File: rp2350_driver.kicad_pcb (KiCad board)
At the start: 6 copper layers, 76 x 44.4 mm, 194 parts, among them J19 Conn_01x03, J201 Estop Conn, J202 USB_C_Receptacle_USB2.0, J203 Conn_01x06, J204 SM03B-SRSS-TB, J206 SM03B-SRSS-TB, J21 Power Input, Q1 Q_PNP_BEC, Q2 Q_PNP_BEC, Q3 Q_PNP_BEC, SW201 Boot, SW202 Reset, U1 INA240A1D, U2 EG3113, U202 SPX3819M5-L-3-3, U203 RP2350_80QFN, U204 W25Q16JV, U205 USBLC6-4SC6, U21 INA240A1D, U44 INA240A1D, U5 EG3113, U8 EG3113, Y201 ABM8-272-T3

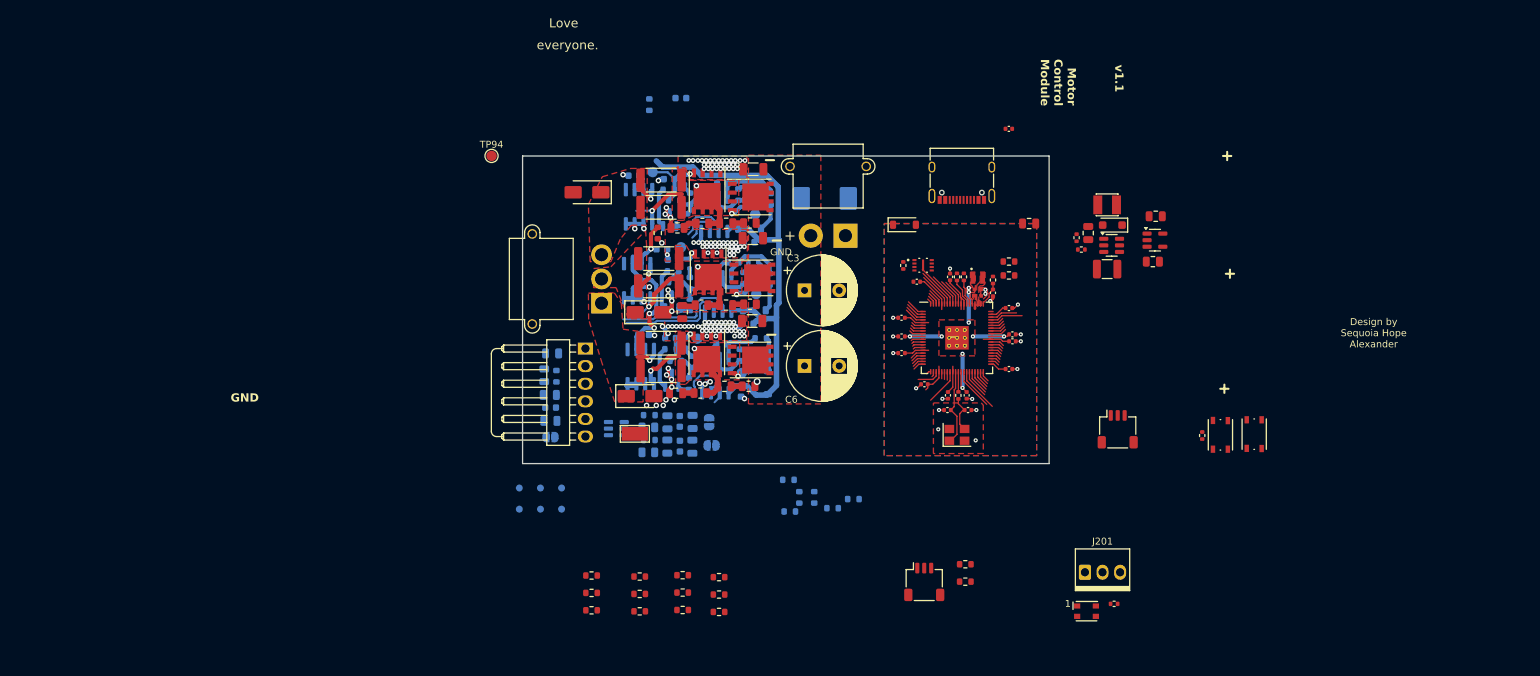
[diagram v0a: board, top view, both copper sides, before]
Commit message: Add 4th bridge, update connectors
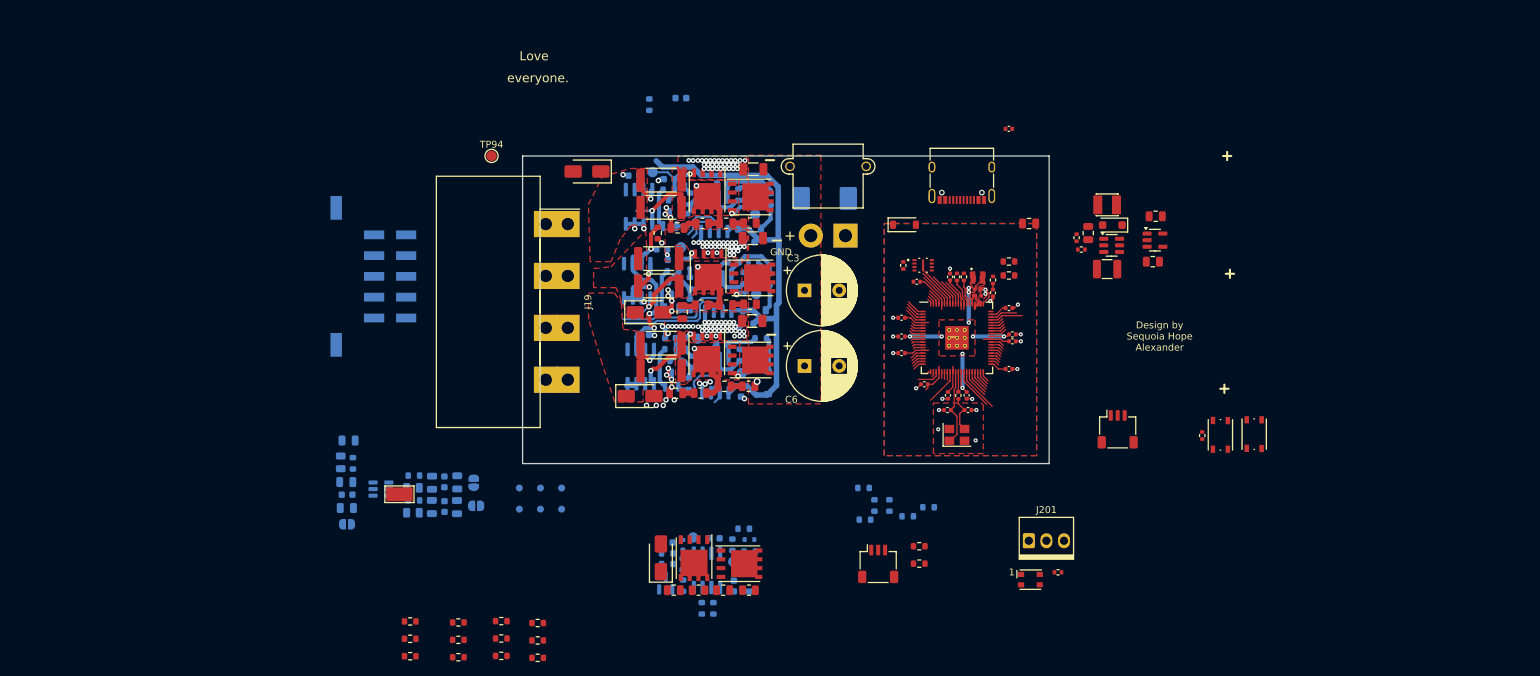
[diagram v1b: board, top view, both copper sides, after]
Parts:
- added C220: 4.7uF 35V, Capacitor_SMD:C_0603_1608Metric, B.Cu at (143.0, 144.1)
- added C233: DNP, Capacitor_SMD:C_0603_1608Metric, B.Cu at (133.4, 137.8)
- added C234: C, Capacitor_SMD:C_0805_2012Metric, F.Cu at (141.4, 144.7)
- added C235: C, Capacitor_SMD:C_0805_2012Metric, F.Cu at (134.3, 144.7)
- added C236: 10uF 35v, Capacitor_SMD:C_0603_1608Metric, B.Cu at (140.2, 137.2)
- added CH201: MOSFETSO-8, parts:PowerPAK_SO-8_123, F.Cu at (143.8, 140.8)
- added CL201: MOSFETSO-8, parts:PowerPAK_SO-8_123, F.Cu at (137.2, 140.1)
- added D203: FR107, Diode_SMD:D_SOD-123, B.Cu at (145.3, 143.2)
- added D204: CDBU0130R-HF, Diode_SMD:D_SOD-523, B.Cu at (145.2, 137.4)
- added D205: CDBU0130R-HF, Diode_SMD:D_SOD-523, B.Cu at (135.6, 138.1)
- added D206: SMAJ51A, Diode_SMD:D_SMA, F.Cu at (132.5, 140.0)
- added Q201: Q_PNP_BEC, Package_TO_SOT_SMD:SOT-23, B.Cu at (133.2, 143.6)
- added R227: 10k, Resistor_SMD:R_0603_1608Metric, B.Cu at (140.0, 147.3)
- added R228: 10k, Resistor_SMD:R_0603_1608Metric, B.Cu at (138.4, 147.3)
- added R229: 0R, Resistor_SMD:R_0603_1608Metric, B.Cu at (144.4, 135.8)
- added R230: 0R, Resistor_SMD:R_0603_1608Metric, B.Cu at (142.8, 138.1)
- added R231: 100R, Resistor_SMD:R_0603_1608Metric, B.Cu at (135.7, 144.0)
- added R232: 0R, Resistor_SMD:R_0603_1608Metric, B.Cu at (135.6, 140.9)
- added R233: 10.2R, Resistor_SMD:R_0603_1608Metric, B.Cu at (133.4, 140.9)
- added R234: 10.2R, Resistor_SMD:R_0603_1608Metric, B.Cu at (145.3, 139.1)
- added R235: 10.2R, Resistor_SMD:R_0603_1608Metric, B.Cu at (133.4, 139.4)
- added R236: R, Resistor_SMD:R_0805_2012Metric, F.Cu at (145.2, 144.7)
- added R237: R, Resistor_SMD:R_0805_2012Metric, F.Cu at (137.9, 144.7)
- added TP207: TestPoint, parts:TestPoint_Pad_D1.5mm_no_courtyard, B.Cu at (142.9, 140.6)
- added TP208: TestPoint, parts:TestPoint_Pad_D1.5mm_no_courtyard, B.Cu at (137.1, 137.1)
- added U201: EG3113, Package_SO:SOIC-8_3.9x4.9mm_P1.27mm, B.Cu at (139.1, 141.8)
- J19: footprint Connector_AMASS:AMASS_MR30PW-M_1x03_P3.50mm_Horizontal -> Connector_Molex:Molex_Sabre_46007-1104_1x04_P7.49mm_Horizontal
- J203: footprint parts:Molex_KK-254_1x06_P2.54mm_Horizontal -> Connector_Molex:Molex_Micro-Fit_3.0_43045-1010_2x05-1MP_P3.00mm_Horizontal; moved to B.Cu
- moved C227 35.1 mm to (103.1, 129.1)
- moved JP202 35.1 mm to (105.5, 129.2)
- moved R216 35.1 mm to (96.8, 128.1)
- moved R218 35.1 mm to (96.8, 131.7)
- moved U205 35.1 mm to (92.1, 130.1)
- moved C228 35.1 mm to (101.2, 129.0)
- moved C229 35.1 mm to (99.4, 129.2)
- moved C232 35.1 mm to (99.4, 132.7)
- moved R217 35.1 mm to (96.7, 129.9)
- moved C230 35.1 mm to (103.0, 132.7)
- moved C231 35.1 mm to (101.2, 132.6)
- moved R219 35.1 mm to (96.7, 133.5)
- moved TP71 35.1 mm to (94.7, 130.8)
- moved JP203 35.1 mm to (105.8, 132.5)
- moved C226 32.0 mm to (87.0, 129.1)
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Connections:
- J203 pad 1: /TH_MOTOR1 -> unconnected-(J203-Pin_1-Pad1)
- J203 pad 2: +3V3 -> unconnected-(J203-Pin_2-Pad2)
- J203 pad 3: /ENC1_RX -> unconnected-(J203-Pin_3-Pad3)
- J203 pad 4: /ENC1_CS -> unconnected-(J203-Pin_4-Pad4)
- J203 pad 5: /ENC1_SCK -> unconnected-(J203-Pin_5-Pad5)
- J203 pad 6: GND -> unconnected-(J203-Pin_6-Pad6)
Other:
- board text removed: "Motor Control Module"
- board text removed: "v1.1"

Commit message: Refine design rules, make cpu fit rules, add gitignore
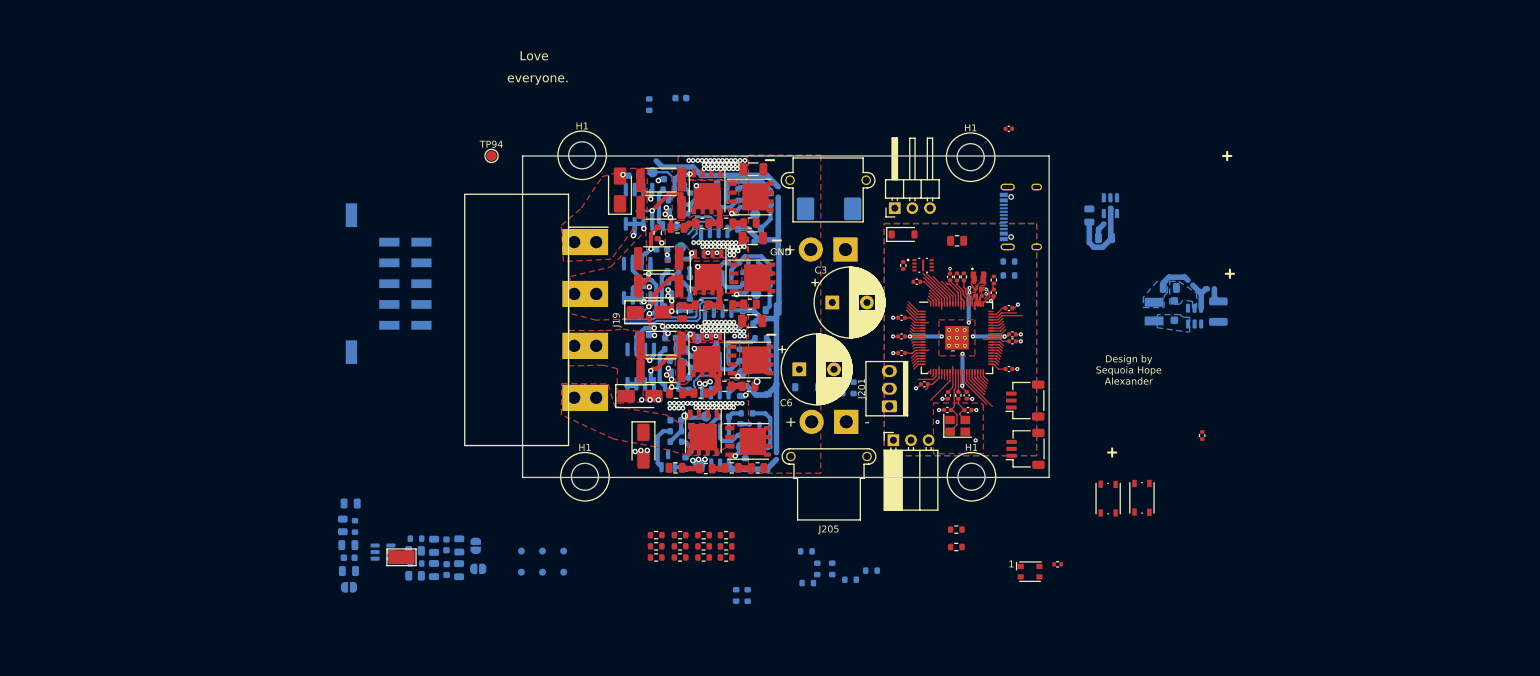
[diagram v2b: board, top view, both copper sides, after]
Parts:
- added D207: 3.3v Zener, Diode_SMD:D_SOD-123, B.Cu at (153.5, 115.4)
- added H1: MountingHole, parts:MountingHole_3.9mm_Plastite_#6, F.Cu at (177.2, 82.2)
- added H1: MountingHole, parts:MountingHole_3.9mm_Plastite_#6, F.Cu at (121.1, 81.9)
- added H1: MountingHole, parts:MountingHole_3.9mm_Plastite_#6, F.Cu at (177.3, 128.3)
- added H1: MountingHole, parts:MountingHole_3.9mm_Plastite_#6, F.Cu at (121.5, 128.3)
- added J205: Power Output, Connector_AMASS:AMASS_XT30PW-F_1x02_P2.50mm_Horizontal, F.Cu at (159.2, 120.4)
- added J207: Conn_01x03, Connector_PinHeader_2.54mm:PinHeader_1x03_P2.54mm_Horizontal, F.Cu at (166.2, 89.5)
- added J208: Conn_01x03, Connector_PinSocket_2.54mm:PinSocket_1x03_P2.54mm_Horizontal, F.Cu at (166.0, 123.0)
- added R238: 50k 0.1%, Resistor_SMD:R_0603_1608Metric, B.Cu at (157.0, 115.5)
- added R239: 50k 0.1%, Resistor_SMD:R_0603_1608Metric, B.Cu at (158.7, 115.5)
- added R240: 5.1k 0.1%, Resistor_SMD:R_0603_1608Metric, B.Cu at (160.3, 115.5)
- C10, C12, C201, C202, D3, J202, L1, R11, R12, R212, R213, U202: moved to B.Cu
- U4: value ~ -> TX4137; moved to B.Cu
- moved R13 38.3 mm to (131.8, 139.9)
- moved R10 37.9 mm to (131.8, 138.3)
- moved R6 37.6 mm to (131.8, 136.7)
- moved R207 35.1 mm to (135.2, 139.9)
- moved R205 34.7 mm to (135.2, 138.3)
- moved R204 34.4 mm to (135.2, 136.7)
- moved R220 32.5 mm to (138.6, 140.0)
- moved R210 32.1 mm to (138.6, 138.3)
- moved R209 31.7 mm to (138.6, 136.7)
- moved R223 30.8 mm to (141.9, 140.0)
- moved R222 30.4 mm to (141.9, 138.3)
- moved R221 30.0 mm to (141.9, 136.7)
- moved J201 28.0 mm to (165.1, 118.1), turned to 90 degrees
- moved J206 27.0 mm to (185.1, 124.3), turned to 90 degrees
- moved R11 19.5 mm to (211.9, 101.2)
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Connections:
- U4 pad 4: unconnected-(U4-EN-Pad4) -> /V_ENABLE
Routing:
- net GND: track 62.4 -> 80.5 mm, vias 150 -> 186
- net +5V: track 73.9 -> 91.6 mm
- net /2DGL: track 0.00 -> 9.13 mm, vias 0 -> 1
- net /2DGH: track 0.00 -> 8.03 mm, vias 0 -> 1
- net Net-(D203-K): track 0.00 -> 7.61 mm
- net Net-(Q201-E): track 0.00 -> 6.78 mm
- net Net-(U201-LO): track 0.00 -> 6.61 mm
- net Net-(U201-HO): track 0.00 -> 6.00 mm
- net Net-(U4-FB): track 0.00 -> 4.99 mm
- net Vdrive: track 0.00 -> 4.80 mm
- net /D: track 0.00 -> 4.39 mm
- net Net-(U201-VB): track 0.00 -> 4.00 mm
- net VMOT: track 4.97 -> 1.15 mm
- net Net-(C235-Pad1): track 0.00 -> 2.55 mm
- net +3V3: track 70.9 -> 73.1 mm
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- added copper zone on F.Cu, net /D
- added copper zone on B.Cu, net Net-(D3-K)
- added copper zone on B.Cu, net Vdrive
- removed copper zone on F.Cu, net (none)
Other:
- board size 76 x 44.4 mm -> 76 x 46.4 mm

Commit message: adjust stackup, rotate CPU, update via and trace defaults
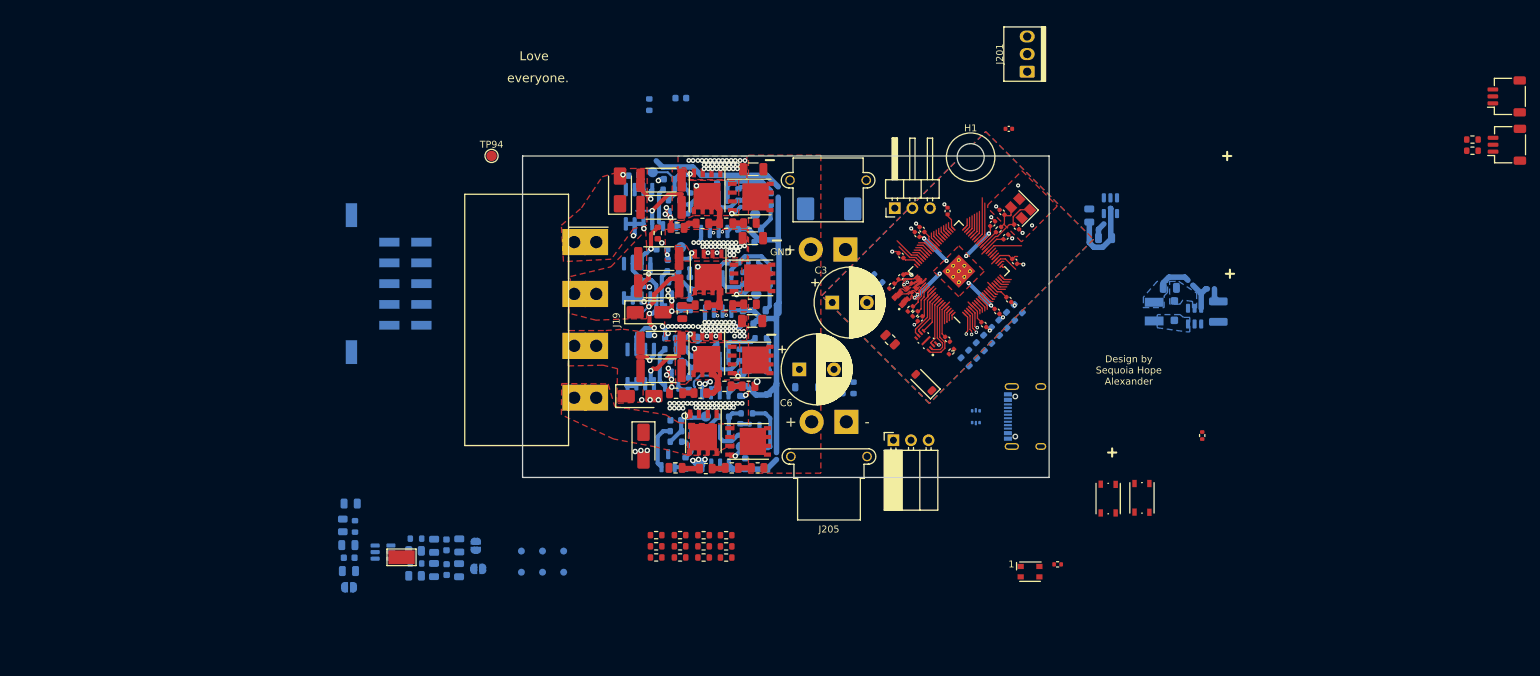
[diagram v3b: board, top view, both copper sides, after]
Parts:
- removed the H1 at (121.1, 81.9)
- removed the H1 at (177.3, 128.3)
- removed the H1 at (121.5, 128.3)
- added U3: USBLC6-2P6, Package_TO_SOT_SMD:SOT-666, B.Cu at (177.9, 119.6)
- moved R225 93.9 mm to (249.6, 81.2)
- moved R224 93.4 mm to (249.6, 79.6)
- moved J206 82.2 mm to (254.6, 80.4)
- moved J204 82.2 mm to (254.6, 73.4)
- moved R227 56.9 mm to (184.0, 104.0), turned to 135 degrees
- moved R228 56.5 mm to (182.9, 105.2), turned to 135 degrees
- moved J201 52.2 mm to (185.0, 69.8)
- moved R123 45.3 mm to (180.8, 107.3), turned to -45 degrees
- moved R124 43.0 mm to (181.8, 106.3), turned to -45 degrees
- moved R121 38.8 mm to (178.6, 109.5), turned to -45 degrees
- moved R122 37.4 mm to (179.6, 108.5), turned to -45 degrees
- moved R119 37.0 mm to (177.5, 110.6), turned to -45 degrees
- moved R120 36.7 mm to (176.4, 111.7), turned to -45 degrees
- moved Y201 32.7 mm to (184.4, 89.6), turned to 135 degrees
- moved C222 29.0 mm to (181.7, 90.1), turned to 135 degrees
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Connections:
- net /GPIO47_ADC7 renamed /TH1_SENSE
- R202 pad 1: /USB_D+ -> /USB_DP
- R203 pad 1: /USB_D- -> /USB_DN
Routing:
- net C_PWM_L\: track 8.40 -> 48.4 mm, vias 0 -> 2
- net C_PWM_H: track 10.5 -> 49.2 mm, vias 0 -> 2
- net B_PWM_L\: track 18.9 -> 45.3 mm, vias 0 -> 2
- net B_PWM_H: track 20.7 -> 42.6 mm, vias 0 -> 2
- net /QSPI_SS: track 5.05 -> 9.65 mm
- net /QSPI_SD3: track 4.01 -> 7.29 mm
- net /QSPI_SD1: track 5.85 -> 9.01 mm
- net /QSPI_SCLK: track 4.04 -> 6.51 mm
- net /QSPI_SD2: track 5.84 -> 7.22 mm
- net GND: track 80.5 -> 81.0 mm, vias 186 -> 187
- net /QSPI_SD0: track 5.06 -> 5.57 mm
- added copper zone on In4.Cu, net GND
- removed copper zone on In2.Cu, net GND

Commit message: refining layout, beginning to sort out differential encoders
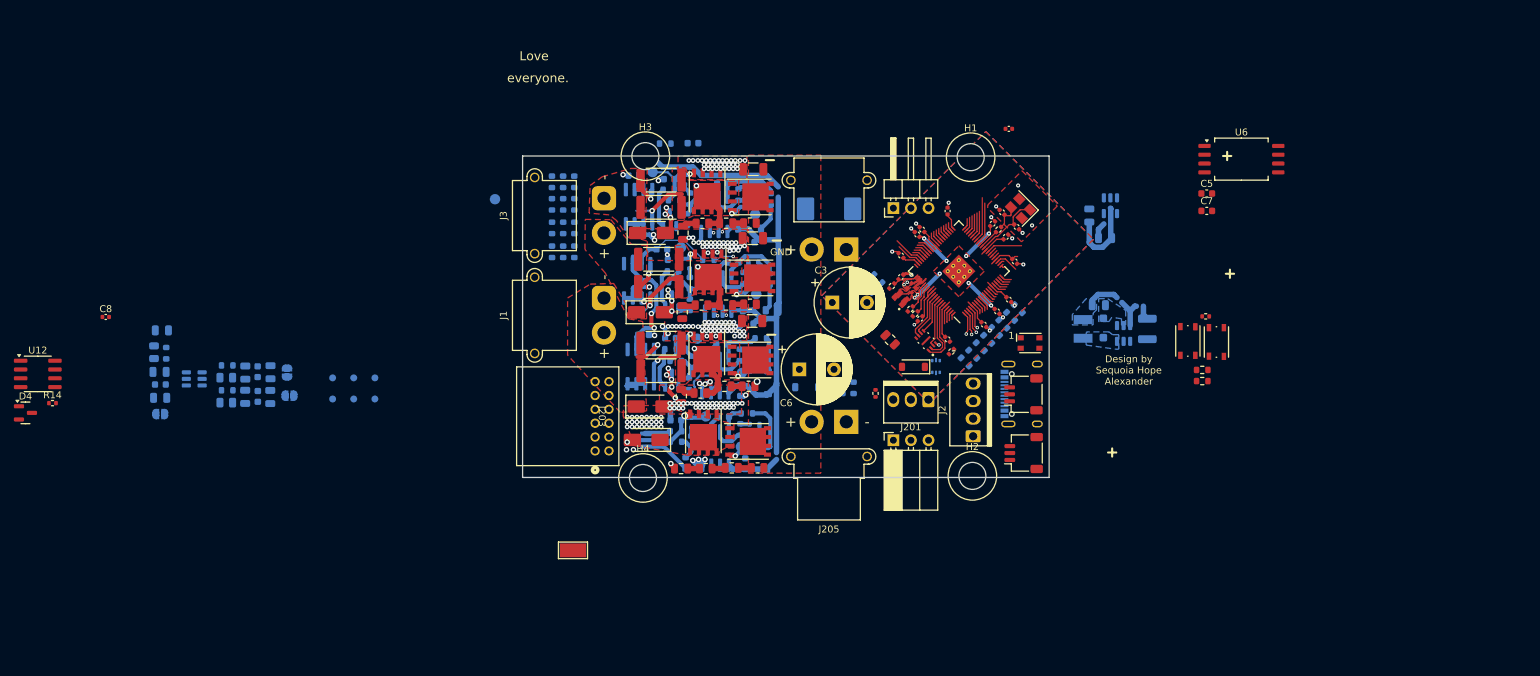
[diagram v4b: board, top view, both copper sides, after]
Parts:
- removed J19: Conn_01x03, Connector_Molex:Molex_Sabre_46007-1104_1x04_P7.49mm_Horizontal
- added C5: 100n, Capacitor_SMD:C_0603_1608Metric, F.Cu at (211.3, 87.4)
- added C7: 4.7uF 35V, Capacitor_SMD:C_0603_1608Metric, F.Cu at (211.3, 89.9)
- added C8: 100n, Capacitor_SMD:C_0402_1005Metric, F.Cu at (52.3, 105.2)
- added D4: ESDCAN24-2BLY, Package_TO_SOT_SMD:SOT-23, F.Cu at (40.7, 119.1)
- added H2: MountingHole, parts:MountingHole_3.9mm_Plastite_#6, F.Cu at (177.4, 128.2)
- added H3: MountingHole, parts:MountingHole_3.9mm_Plastite_#6, F.Cu at (130.2, 82.0)
- added H4: MountingHole, parts:MountingHole_3.9mm_Plastite_#6, F.Cu at (129.9, 128.5)
- added J1: Power Input, Connector_AMASS:AMASS_XT30PW-M_1x02_P2.50mm_Horizontal, F.Cu at (124.2, 102.5)
- added J2: CAN2 PLUG, parts:PINREX-744-81-04TW00 _1x04_P2.54mm_Vertical, F.Cu at (177.2, 122.5)
- added J3: Power Input, Connector_AMASS:AMASS_XT30PW-M_1x02_P2.50mm_Horizontal, F.Cu at (124.2, 88.1)
- added R14: 100R 0402, Resistor_SMD:R_0402_1005Metric, F.Cu at (44.6, 117.7)
- added U12: MAX3485, Package_SO:SOIC-8_3.9x4.9mm_P1.27mm, F.Cu at (42.5, 113.5)
- added U6: CA-IS3052G, Package_SO:SOIC-8_7.5x5.85mm_P1.27mm, F.Cu at (216.3, 82.5)
- J203: footprint Connector_Molex:Molex_Micro-Fit_3.0_43045-1010_2x05-1MP_P3.00mm_Horizontal -> parts:CONN12_5018761240_MOL; moved to F.Cu
- R10, R13, R204, R205, R207, R209, R210, R220, R221, R222, R223, R6, TH1, TP94: moved to B.Cu
- moved J206 82.7 mm to (184.8, 124.9)
- moved J204 81.9 mm to (184.8, 116.4)
- moved R223 59.8 mm to (116.7, 85.7), turned to 90 degrees
- moved R222 57.6 mm to (118.3, 85.7), turned to 90 degrees
- moved R221 55.5 mm to (120.0, 85.7), turned to 90 degrees
- moved R220 55.5 mm to (116.7, 89.0), turned to 90 degrees
- moved R210 53.4 mm to (118.4, 89.0), turned to 90 degrees
- moved R209 51.3 mm to (120.0, 89.0), turned to 90 degrees
- moved R224 51.2 mm to (210.6, 112.9)
- moved R225 51.2 mm to (210.6, 114.5)
- moved R207 51.0 mm to (116.8, 92.4), turned to 90 degrees
- moved J201 49.7 mm to (171.1, 117.5), turned to 180 degrees
- moved R205 49.0 mm to (118.4, 92.4), turned to 90 degrees
- moved R204 46.9 mm to (120.0, 92.4), turned to 90 degrees
- moved R13 46.6 mm to (116.8, 95.8), turned to 90 degrees
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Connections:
- J207 pad 1: unconnected-(J207-Pin_1-Pad1) -> /TXO_INTERBOARD_1
- J207 pad 2: unconnected-(J207-Pin_2-Pad2) -> /RXI_INTERBOARD_1
- J207 pad 3: unconnected-(J207-Pin_3-Pad3) -> GND
- J208 pad 1: unconnected-(J208-Pin_1-Pad1) -> /RXI_INTERBOARD_2
- J208 pad 2: unconnected-(J208-Pin_2-Pad2) -> /TXO_INTERBOARD_2
- J208 pad 3: unconnected-(J208-Pin_3-Pad3) -> GND
- U203 pad 11: /GPIO12 -> /TXO_INTERBOARD_1
- U203 pad 12: /GPIO13 -> /RXI_INTERBOARD_1
- U203 pad 20: /GPIO20 -> /CAN_CPU_TXO
- U203 pad 21: /GPIO21 -> /CAN_CPU_RXI
- U203 pad 25: /GPIO24 -> /TXO_INTERBOARD_2
- U203 pad 26: /GPIO25 -> /RXI_INTERBOARD_2
- U203 pad 6: /CAN_TXO -> D_PWM_H
- U203 pad 7: /CAN_RXI -> D_PWM_L\
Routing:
- net GND: track 81.0 -> 92.0 mm, vias 187 -> 186
- net Net-(Q201-B): track 1.68 -> 7.25 mm
- net +3V3: track 73.1 -> 78.4 mm, vias 3 -> 2
- net Net-(Q201-E): track 6.78 -> 3.77 mm
- net /TH1_SENSE: track 4.79 -> 6.90 mm
- net D_PWM_L\: track 0.00 -> 1.86 mm
- net /CAN_RXI: track 1.86 -> 0.00 mm
- net /TXO_INTERBOARD_1: track 0.00 -> 1.79 mm
- net /GPIO12: track 1.79 -> 0.00 mm
- net D_PWM_H: track 0.00 -> 1.77 mm
- net /CAN_TXO: track 1.77 -> 0.00 mm
- net /RXI_INTERBOARD_1: track 0.00 -> 1.69 mm
- net /GPIO13: track 1.69 -> 0.00 mm
- net /GPIO20: track 1.59 -> 0.00 mm
- net /CAN_CPU_TXO: track 0.00 -> 1.59 mm
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- added copper zone on In2.Cu, net /D
